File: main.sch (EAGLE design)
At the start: 50 parts, among them U1 SN65HVD10_D_8

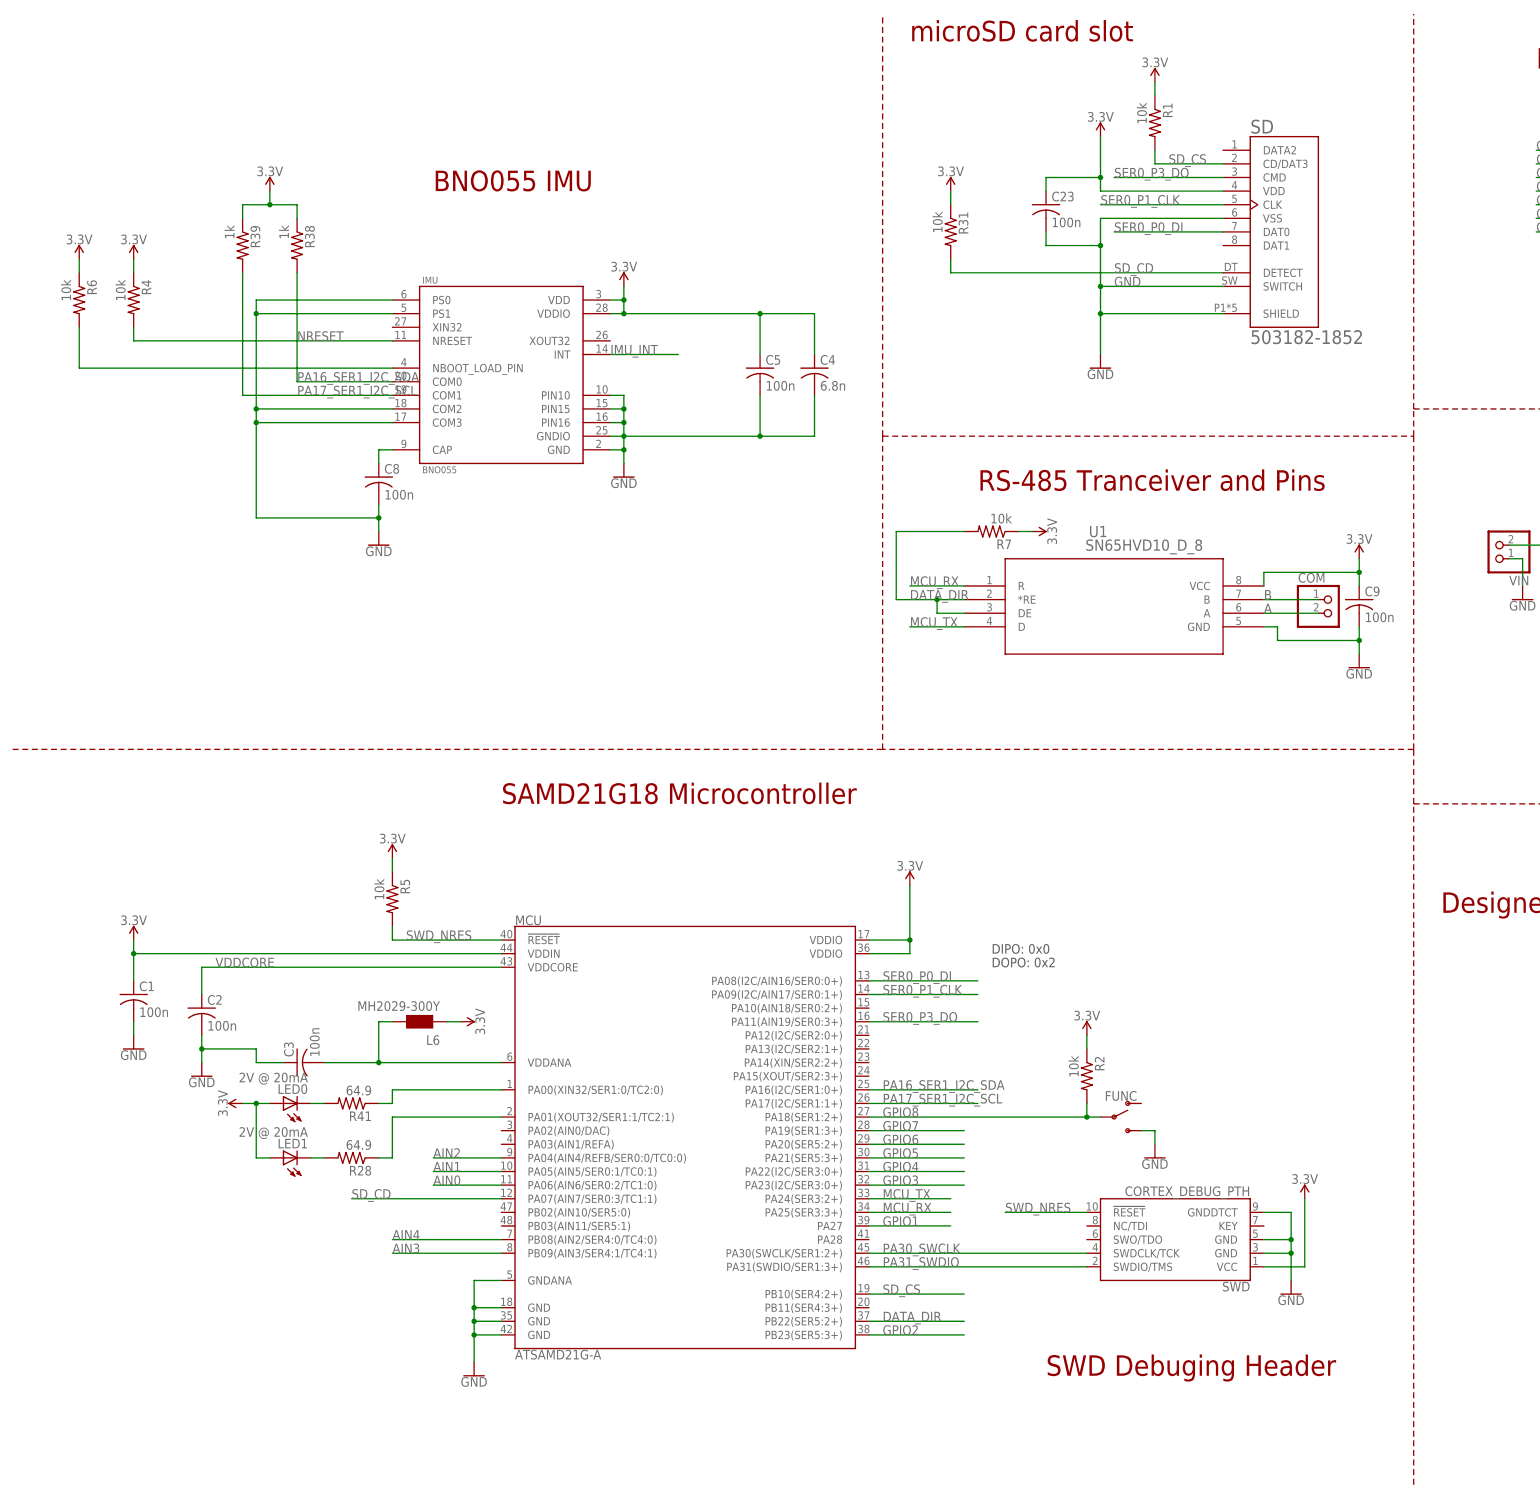
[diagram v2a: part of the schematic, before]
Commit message: Switched out SWD header for one with bigger drills
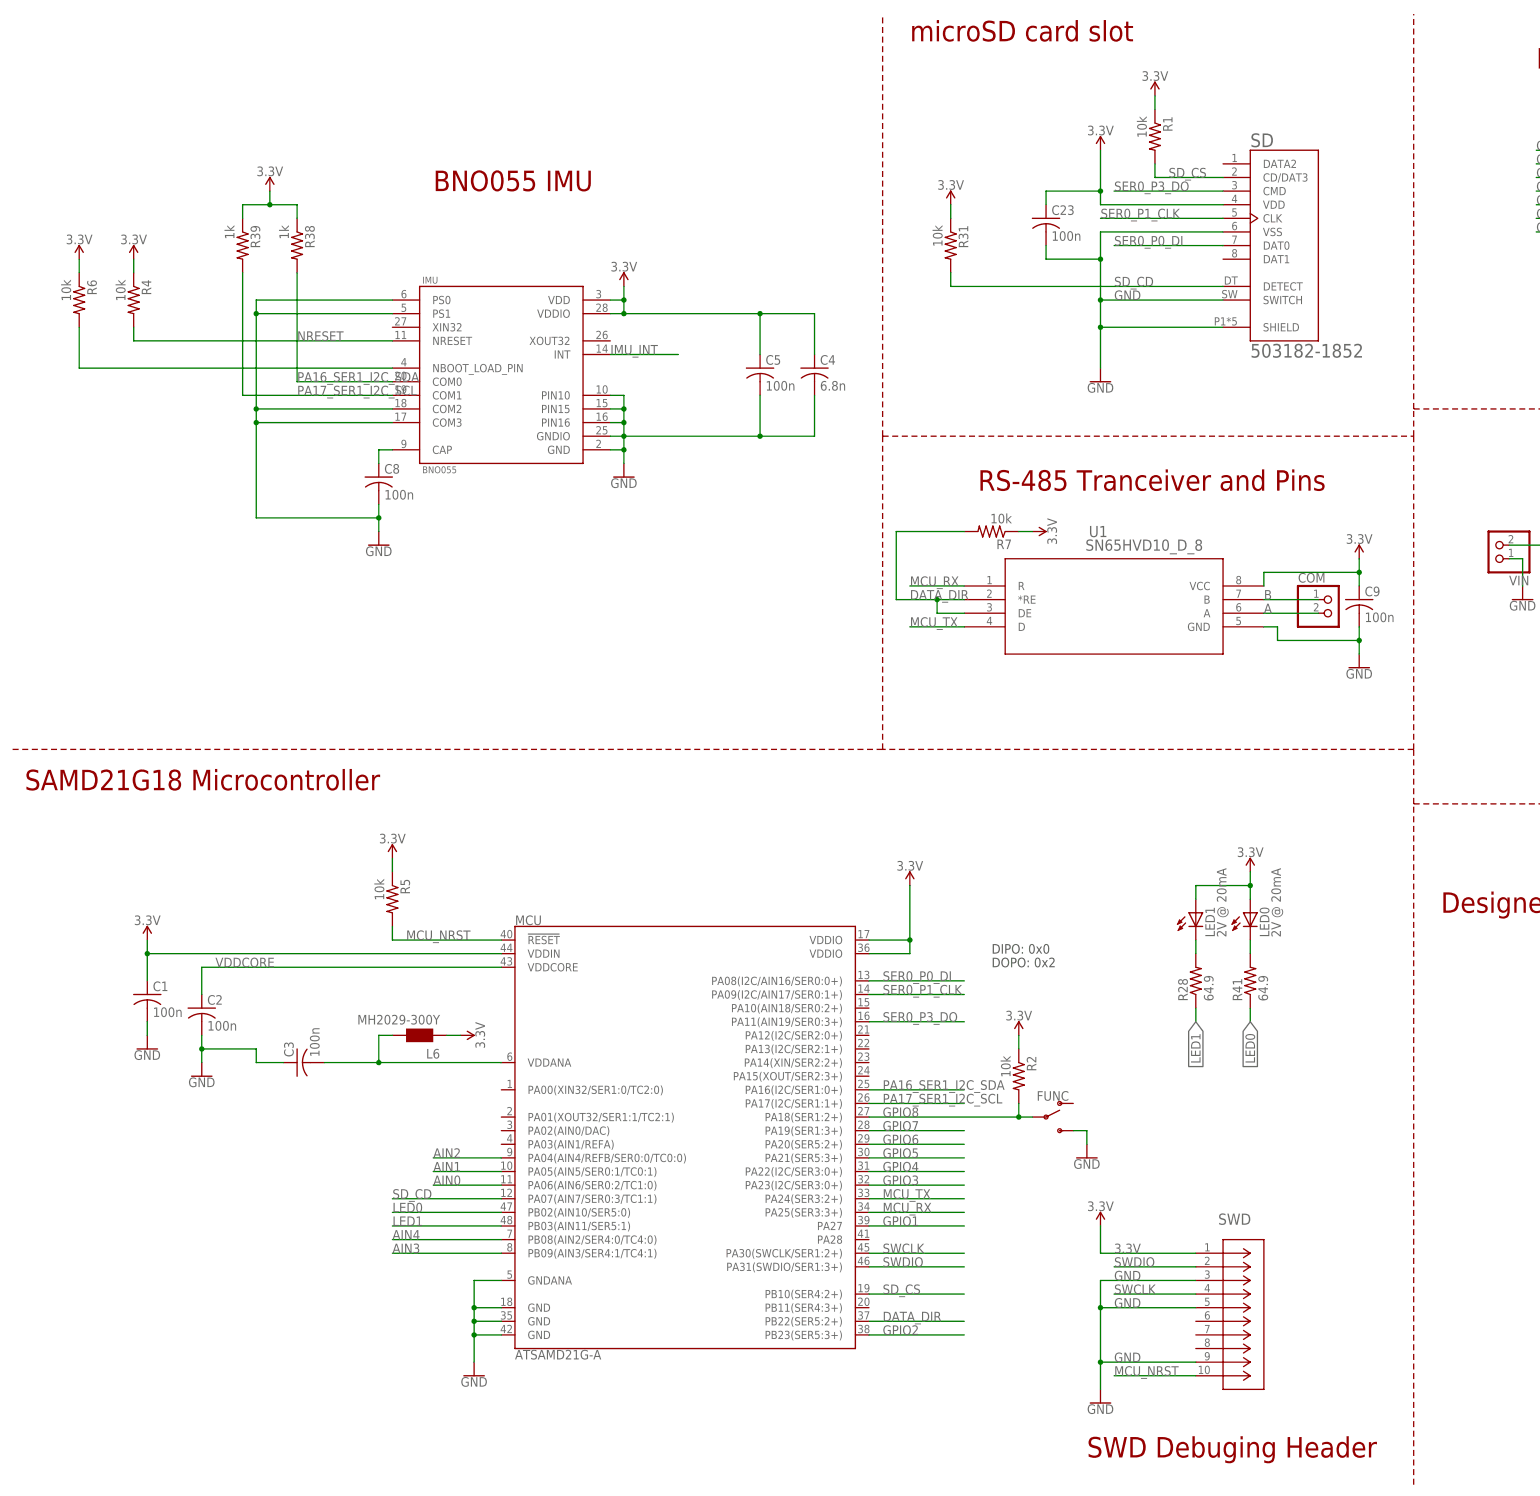
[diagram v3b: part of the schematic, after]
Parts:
- SWD: value CORTEX_DEBUG_PTH -> DEBUG-HEADER; device SparkFun-Connectors:CORTEX_DEBUG_PTH -> senior-design-custom:DEBUG-HEADER
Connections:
- removed net N$14: MCU.PA01(XOUT32/SER1:1/TC2:1), R28.1
- removed net N$16: MCU.PA00(XIN32/SER1:0/TC2:0), R41.1
- removed net PA30_SWCLK: MCU.PA30(SWCLK/SER1:2+), SWD.SWDCLK/TCK
- removed net PA31_SWDIO: MCU.PA31(SWDIO/SER1:3+), SWD.SWDIO/TMS
- removed net SWD_NRES: MCU.!RESET!, R5.2, SWD.!RESET
- new net LED0: MCU.PB02(AIN10/SER5:0), R41.1
- new net LED1: MCU.PB03(AIN11/SER5:1), R28.1
- new net MCU_NRST: MCU.!RESET!, R5.2, SWD.10
- new net SWCLK: MCU.PA30(SWCLK/SER1:2+), SWD.4
- new net SWDIO: MCU.PA31(SWDIO/SER1:3+), SWD.2
- net 3.3V: now also SWD.1; no longer SWD.VCC
- net GND: now also SWD.3, SWD.5, SWD.9; no longer SWD.GND@3, SWD.GND@5, SWD.GNDDTCT
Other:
- moved on the sheet: C1, C23, FUNC, L6, LED0, LED1, R1, R2, R28, R31, R41, SD

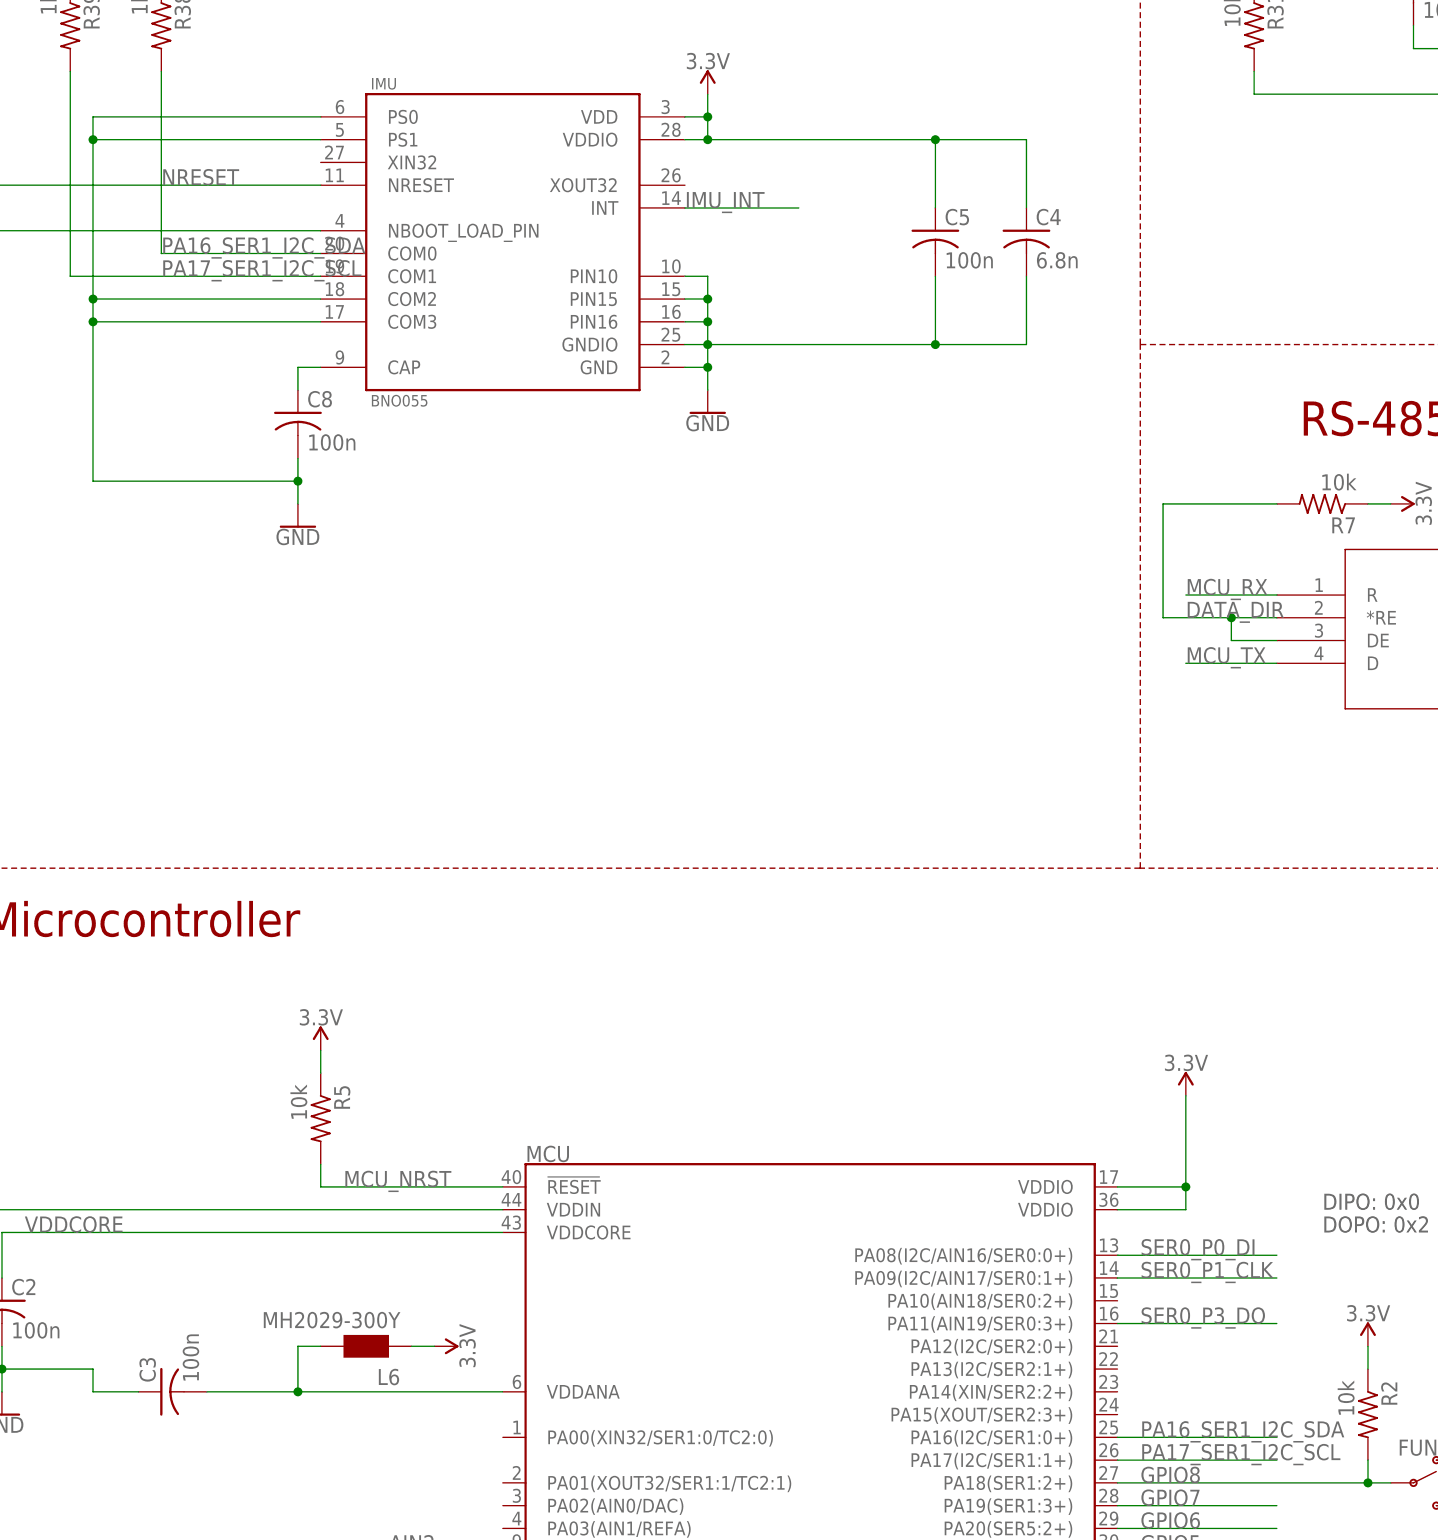
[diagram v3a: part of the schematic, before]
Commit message: Added some traces, added a reset signal to IMU
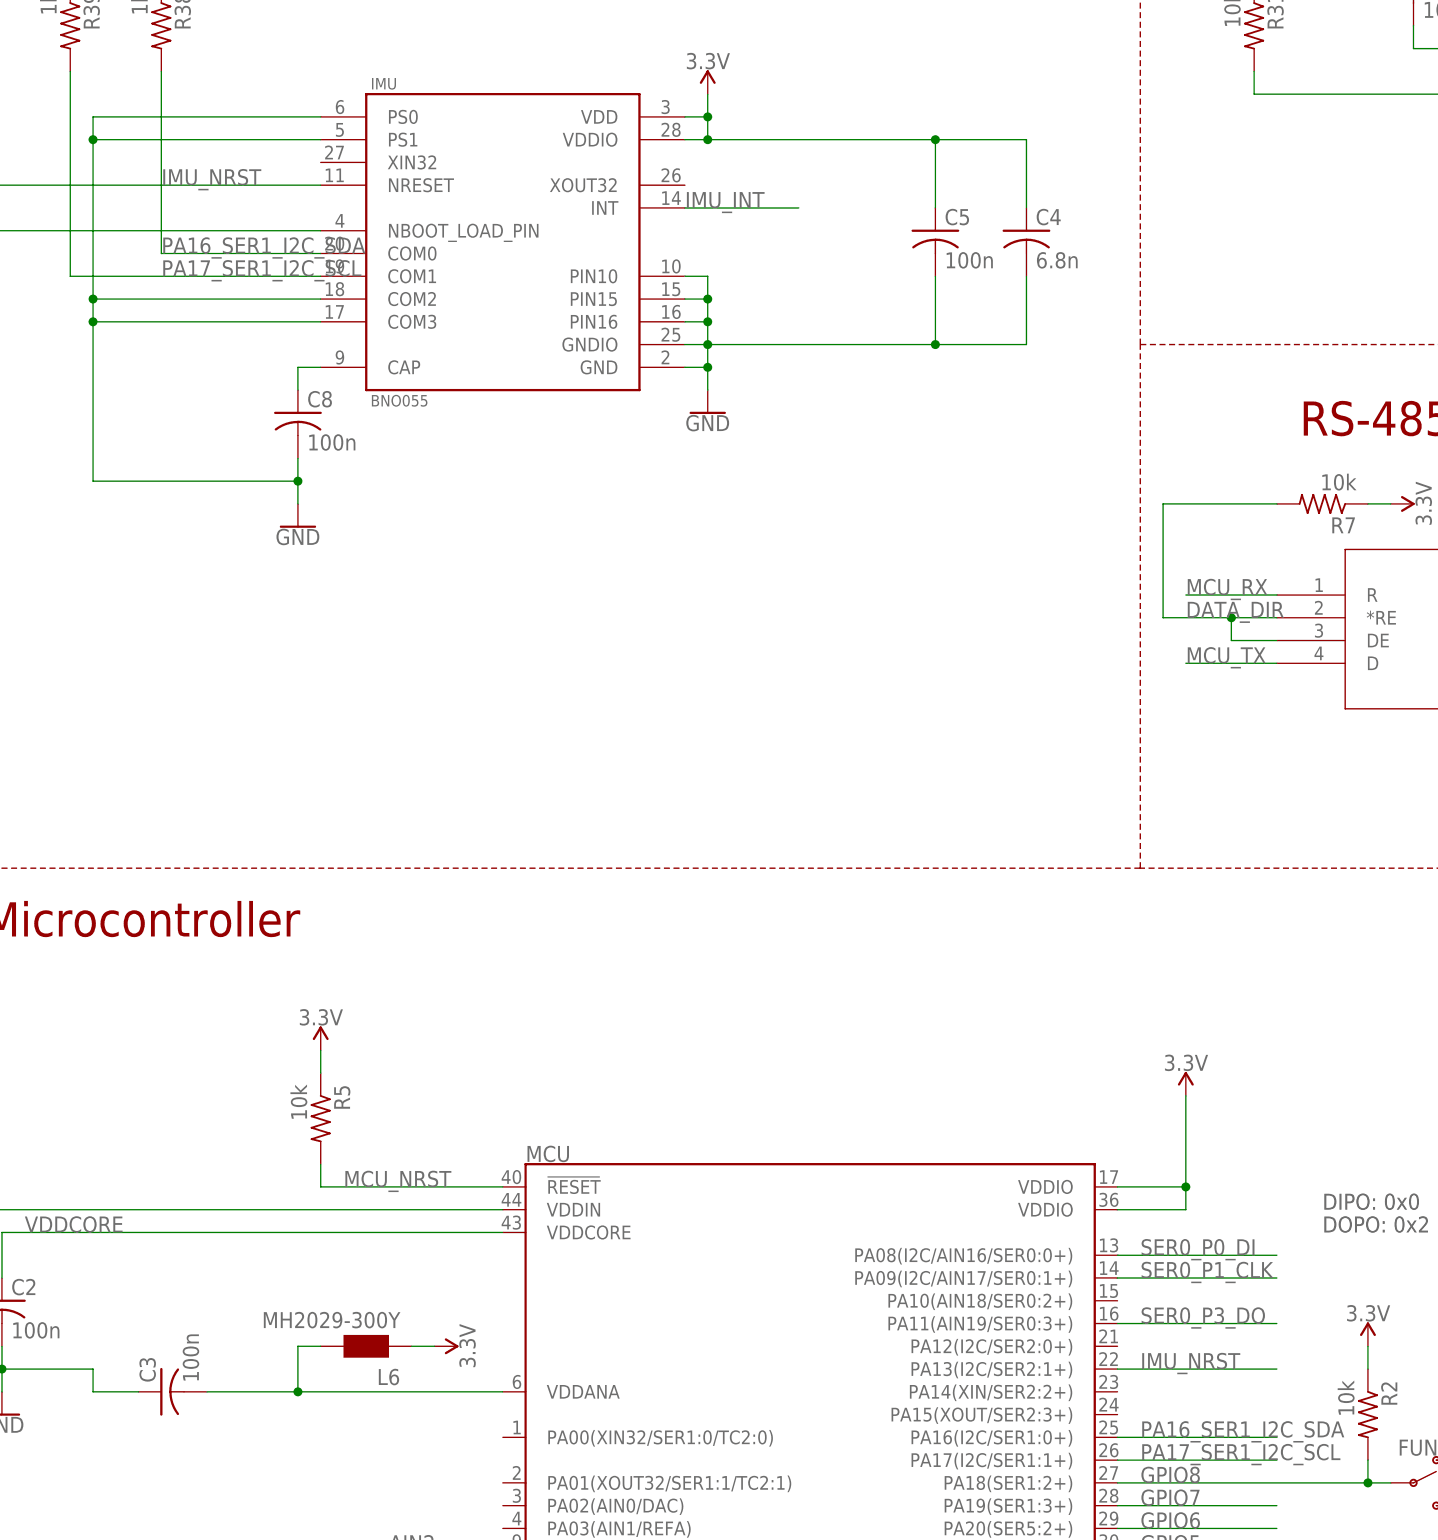
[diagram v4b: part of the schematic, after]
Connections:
- removed net NRESET: IMU.NRESET, R4.2
- new net IMU_NRST: IMU.NRESET, MCU.PA13(I2C/SER2:1+), R4.2
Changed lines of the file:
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@@
 <?xml version="1.0" encoding="utf-8"?>
 <!DOCTYPE eagle SYSTEM "eagle.dtd">
-<eagle version="8.7.1">
+<eagle version="9.0.0">
 <drawing>
 <settings>
@@
 </segment>
 </net>
-<net name="NRESET" class="0">
-<segment>
-<pinref part="IMU" gate="G$1" pin="NRESET"/>
-<label x="58.42" y="213.36" size="1.778" layer="95"/>
-<wire x1="76.2" y1="213.36" x2="27.94" y2="213.36" width="0.1524" layer="91"/>
-<wire x1="27.94" y1="213.36" x2="27.94" y2="215.9" width="0.1524" layer="91"/>
-<pinref part="R4" gate="G$1" pin="2"/>
-</segment>
-</net>
 <net name="N$15" class="0">
 <segment>
@@
 </segment>
 </net>
+<net name="IMU_NRST" class="0">
+<segment>
+<pinref part="MCU" gate="G$1" pin="PA13(I2C/SER2:1+)"/>
+<wire x1="165.1" y1="81.28" x2="182.88" y2="81.28" width="0.1524" layer="91"/>
+<label x="167.64" y="81.28" size="1.778" layer="95"/>
+</segment>
+<segment>
+<pinref part="IMU" gate="G$1" pin="NRESET"/>
+<label x="58.42" y="213.36" size="1.778" layer="95"/>
+<wire x1="76.2" y1="213.36" x2="27.94" y2="213.36" width="0.1524" layer="91"/>
+<wire x1="27.94" y1="213.36" x2="27.94" y2="215.9" width="0.1524" layer="91"/>
+<pinref part="R4" gate="G$1" pin="2"/>
+</segment>
+</net>
